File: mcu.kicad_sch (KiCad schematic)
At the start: 1 part, among them U1 STM32H725ZETx

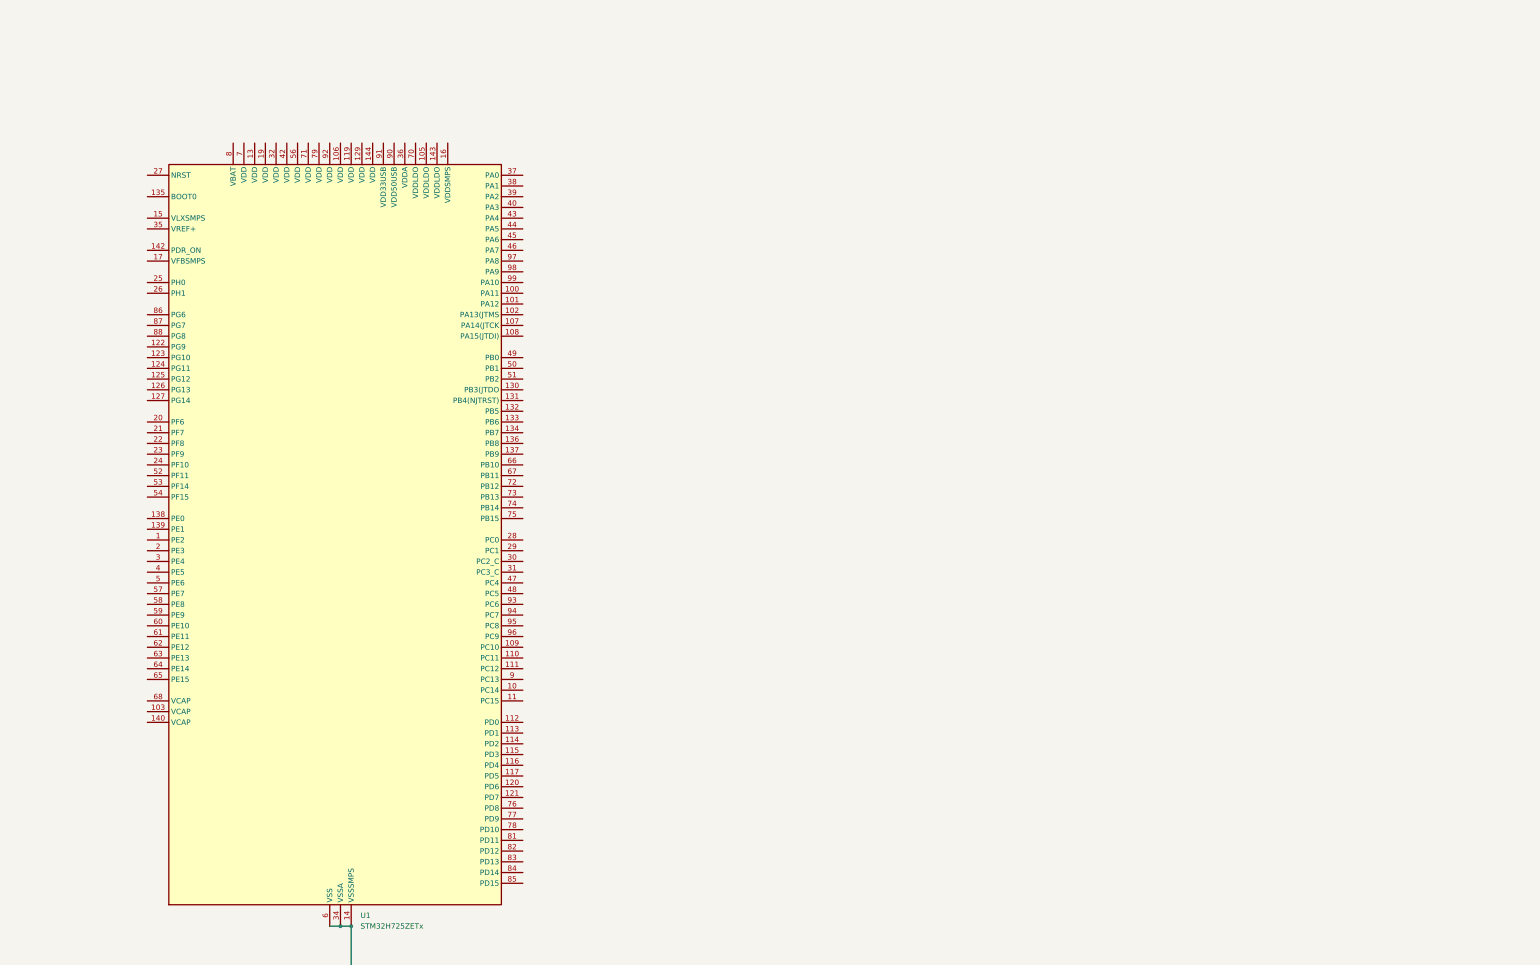
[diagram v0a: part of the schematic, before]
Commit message: working on the stm32 power scheme
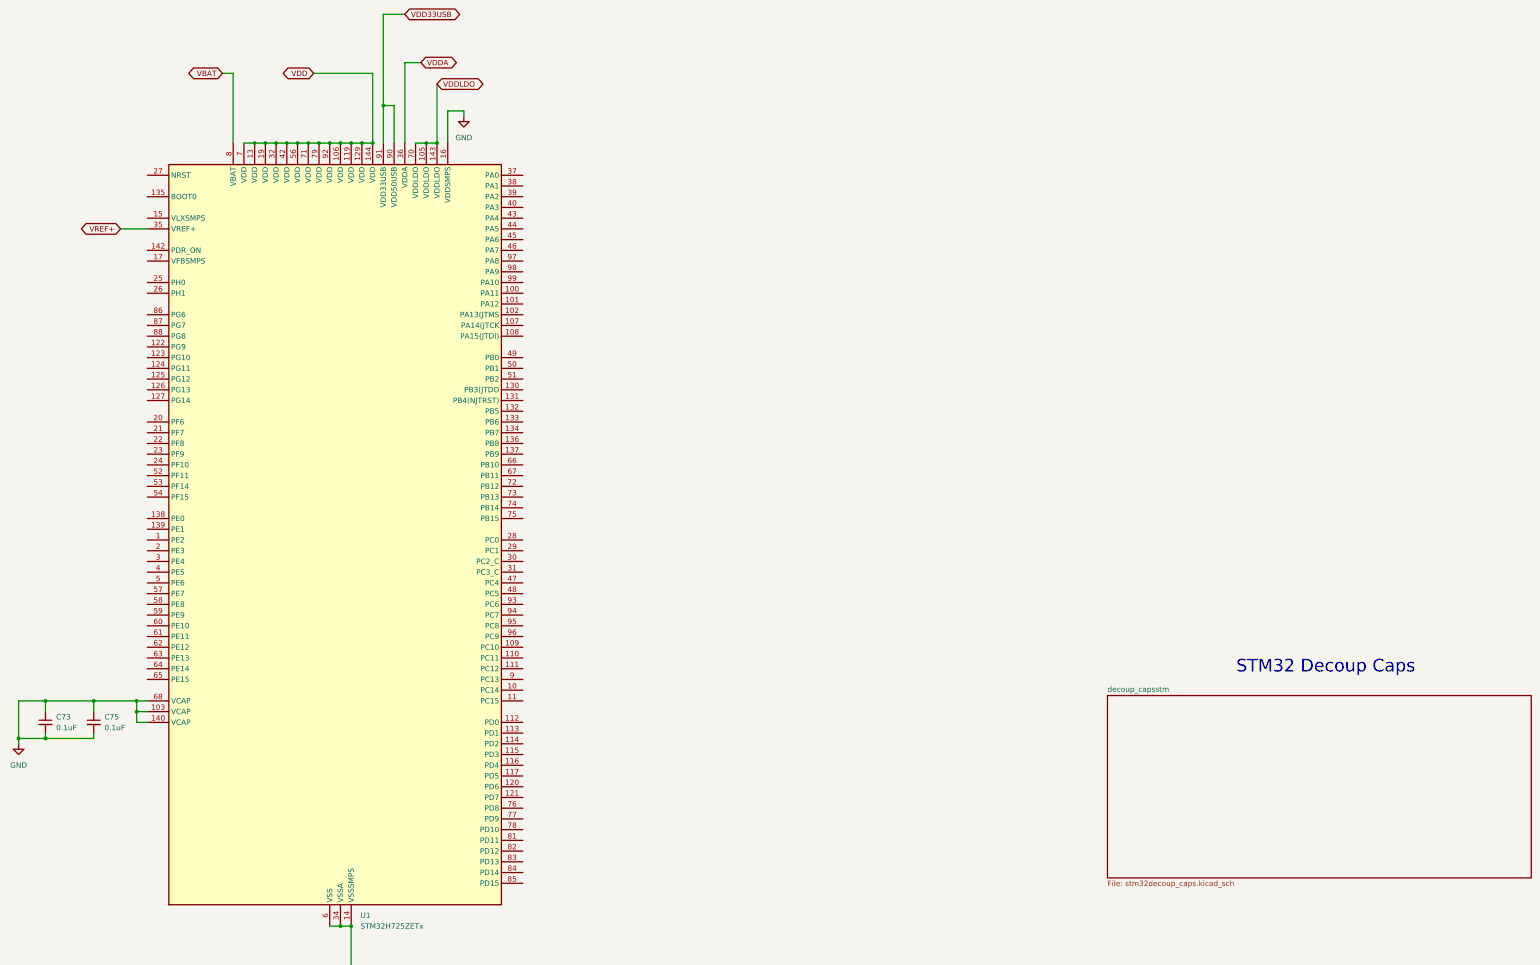
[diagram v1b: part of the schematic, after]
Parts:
- added C73, C75: 0.1uF, Capacitor_SMD:C_0603_1608Metric, symbol Device:C_Small
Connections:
- net GND: now also U1.103 (VCAP), U1.140 (VCAP), U1.16 (VDDSMPS), U1.68 (VCAP), C73.1, C73.2, C75.1, C75.2
- net VDDLDO: now reaches U1.105 (VDDLDO)
- net VDDLDO: now also U1.143 (VDDLDO), U1.70 (VDDLDO)
- net VDD: now reaches U1.106 (VDD)
- net VDD: now also U1.119 (VDD), U1.129 (VDD), U1.13 (VDD), U1.144 (VDD), U1.19 (VDD), U1.32 (VDD), U1.42 (VDD), U1.56 (VDD), U1.7 (VDD), U1.71 (VDD), U1.79 (VDD), U1.92 (VDD)
- net VREF+: now reaches U1.35 (VREF+)
- net VDDA: now reaches U1.36 (VDDA)
- net VBAT: now reaches U1.8 (VBAT)
- net VDD33USB: now reaches U1.90 (VDD50USB)
- net VDD33USB: now also U1.91 (VDD33USB)
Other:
- added sheet decoup_capsstm (stm32decoup_caps.kicad_sch)
- note added: "STM32 Decoup Caps"

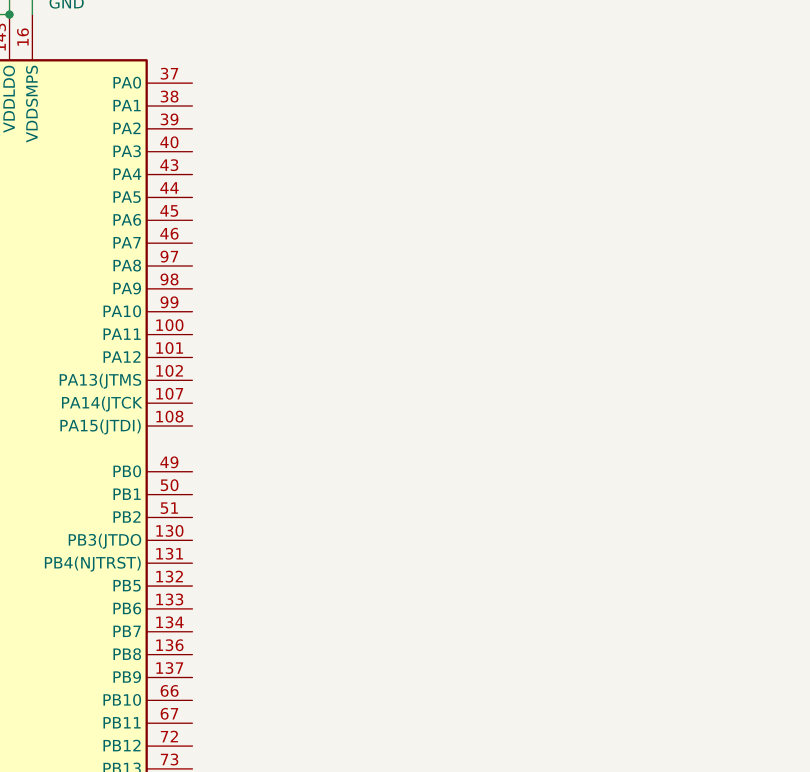
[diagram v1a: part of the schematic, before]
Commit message: SPI for rf chip DW and MCU, finding a SP8T or SP4T
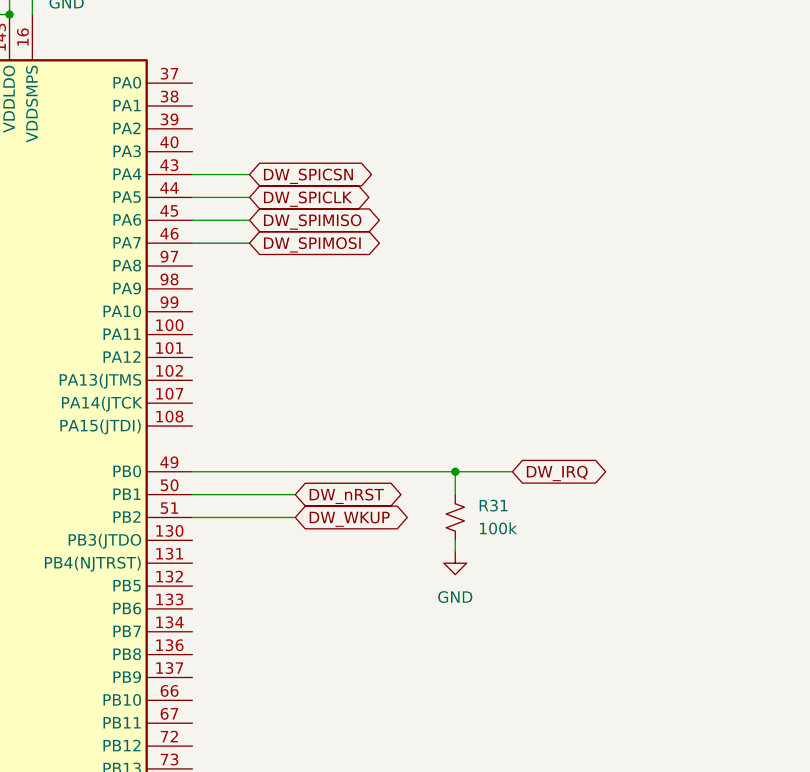
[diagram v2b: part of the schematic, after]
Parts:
- added R31: 100k, Resistor_SMD:R_0603_1608Metric, symbol Device:R_Small_US
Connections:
- net GND: now also R31.2
- net DW_SPICSN: now reaches U1.43 (PA4)
- net DW_SPICLK: now reaches U1.44 (PA5)
- net DW_SPIMISO: now reaches U1.45 (PA6)
- net DW_SPIMOSI: now reaches U1.46 (PA7)
- net DW_IRQ: now reaches U1.49 (PB0)
- net DW_IRQ: now also R31.1
- net DW_nRST: now reaches U1.50 (PB1)
- net DW_WKUP: now reaches U1.51 (PB2)

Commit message: finishing mcu design schematic
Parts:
- added C76: 0.1uF, Capacitor_SMD:C_0603_1608Metric, symbol Device:C_Small
- added R32, R33, R34, R35, R36: 10k, Resistor_SMD:R_0603_1608Metric, symbol Device:R_Small_US
- added SW1: 09.03290.01, symbol Switch:SW_SPDT
- added SW2: SWT0220-016016GSA, symbol Switch:SW_MEC_5E
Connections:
- net GND: now also U1.15 (VLXSMPS), U1.17 (VFBSMPS), C76.1, SW1.1 (A), SW2.1, SW2.2
- net VDD: now also R32.1, R33.2, R34.1, R36.2, SW1.3 (C)
- net ST_JTMS/SWDIO: now reaches U1.102 (PA13(JTMS)
- net ST_JTCLK: now reaches U1.107 (PA14(JTCK)
- net BQ_SCL: now reaches U1.133 (PB6)
- net BQ_SCL: now also R33.1
- net BQ_SDA: now reaches U1.134 (PB7)
- net BQ_SDA: now also R32.2
- net at U1.135 (BOOT0): now also R35.1
- net BQ_CHRG_OK: now reaches U1.136 (PB8)
- net BQ_CHRG_OK: now also R34.2
- net at U1.142 (PDR_ON): now also R36.1
- net ST_NRST: now reaches U1.27 (NRST)
- net ST_NRST: now also C76.2, SW2.3 (K), SW2.4 (A)
- net SW_USART2_TX: now reaches U1.39 (PA2)
- net SW_USART2_RX: now reaches U1.40 (PA3)
- new net: R35.2, SW1.2 (B)
- no-connect marks 0 -> 69
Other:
- moved on the sheet: R31

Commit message: no connects on mcu and D+, D- on connector, ILIM_HIZ voltage divider controls input current
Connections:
- no-connect marks 69 -> 85

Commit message: adding prochot to design, clearing ERC
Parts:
- added R38: 10k, Resistor_SMD:R_0603_1608Metric, symbol Device:R_Small_US
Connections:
- net VDD: now also R38.1
- net BQ_PROCHOT: now reaches U1.137 (PB9)
- net BQ_PROCHOT: now also R38.2
- no-connect marks 85 -> 84
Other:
- moved on the sheet: R31

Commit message: adding all footprints moving onto pcb
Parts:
- SW1: footprint (none) -> Capacitor_SMD:C_0603_1608Metric

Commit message: fixed GS_VBUS overtaking the GND symbol error, lesson learned, fixed PCB ratnest
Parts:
- SW1: footprint Capacitor_SMD:C_0603_1608Metric -> 09111:090329001
- SW2: footprint (none) -> gsb_usb:GSB

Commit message: some changes to schematic nets, grouping passives and mosfets around our charger ic in pcb editor
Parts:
- SW2: footprint gsb_usb:GSB -> button:SWT0220016016GSA
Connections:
- net GND: no longer C73.1, C75.1, U1.103 (VCAP), U1.140 (VCAP), U1.68 (VCAP)
- new net: C73.1, C75.1, U1.103 (VCAP), U1.140 (VCAP), U1.68 (VCAP)
